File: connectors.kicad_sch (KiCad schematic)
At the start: 9 parts, among them J7001 PinHeader_1x3_P2.54mm_SMD, J7002 PinHeader_1x3_P2.54mm_SMD, J7003 Tag-Connect_TC2050-IDC-NL_2x5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

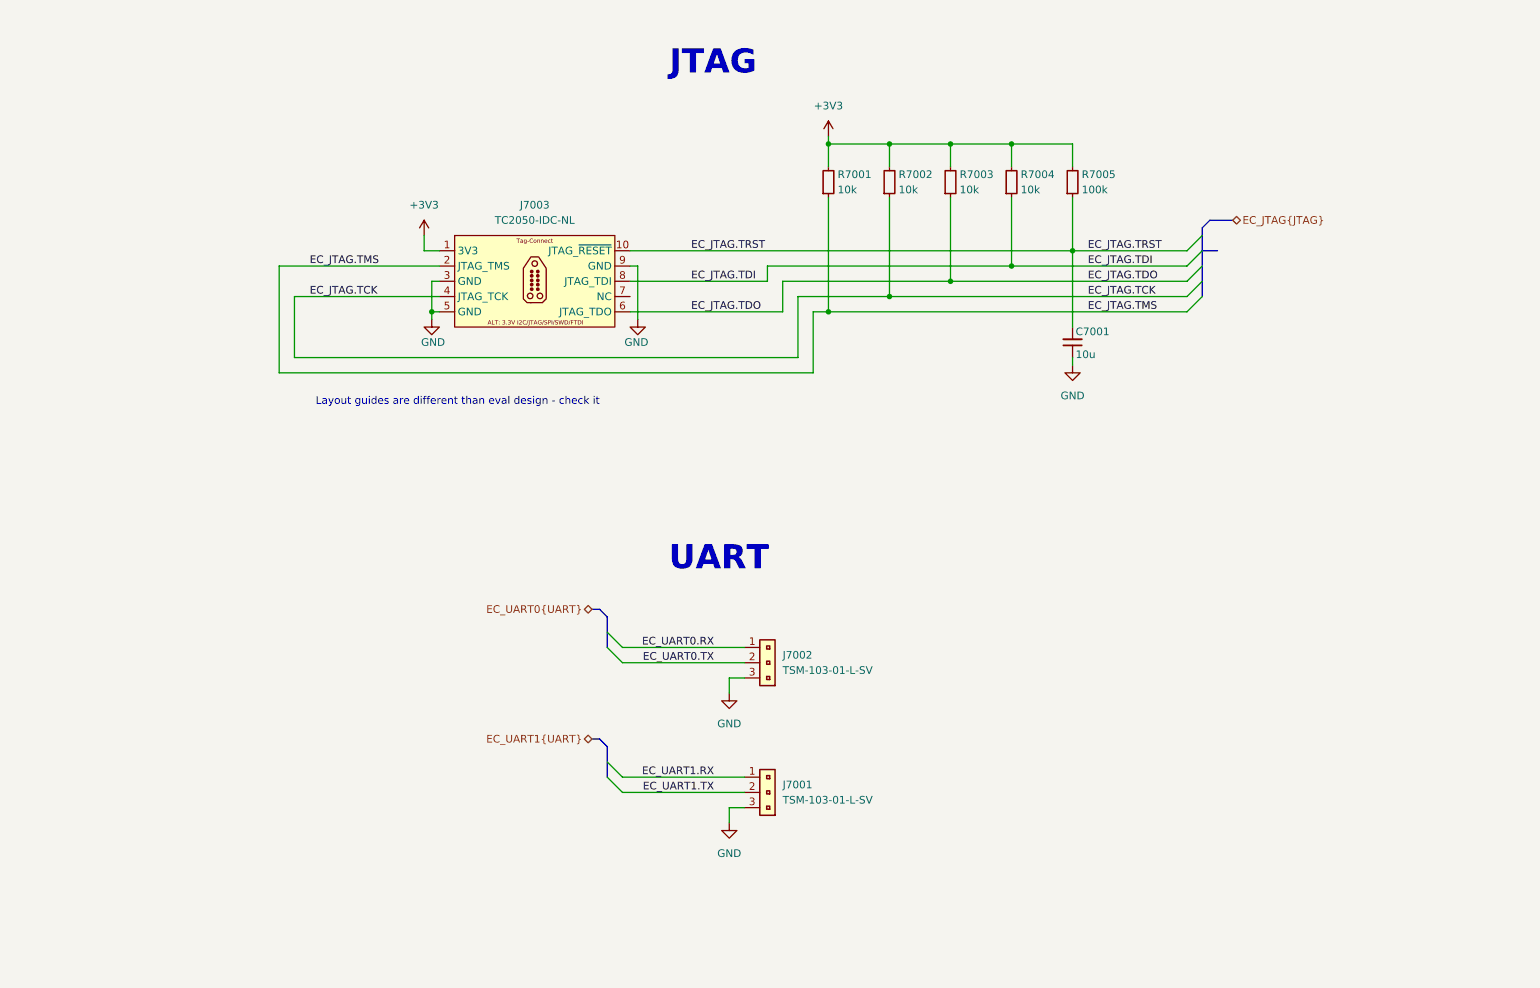
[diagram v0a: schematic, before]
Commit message: [103224] Add USB with FT232RL, transfer elements onto PCB, start positioning elements
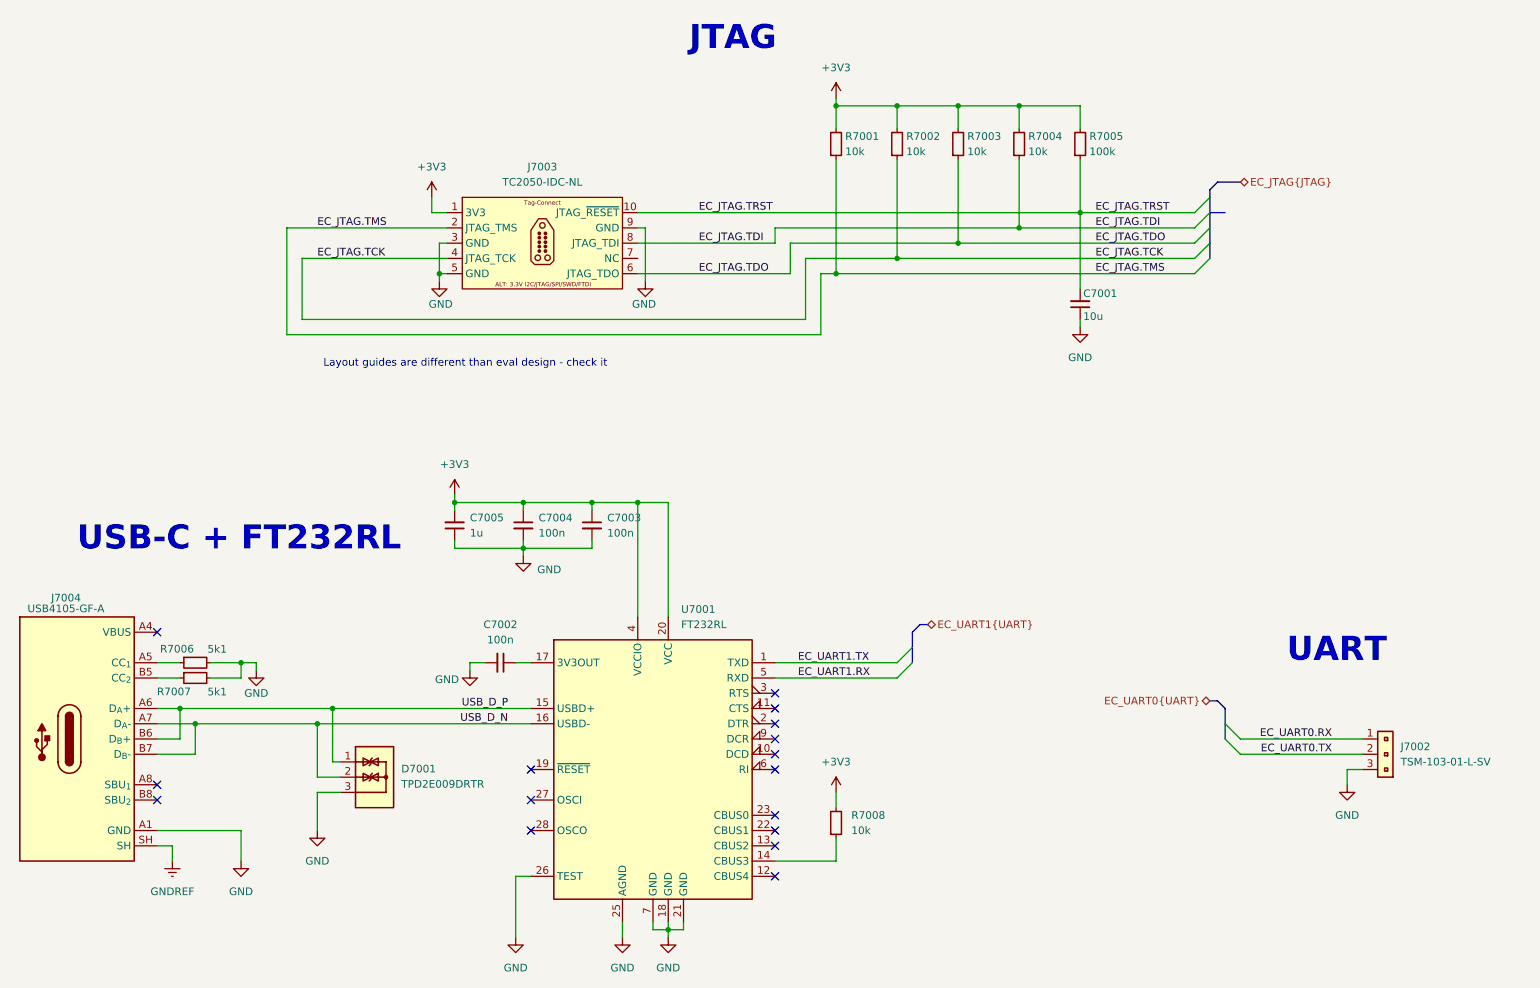
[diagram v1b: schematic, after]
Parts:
- removed J7001: PinHeader_1x3_P2.54mm_SMD, antmicro-footprints:PinHeader_1x3_P2.54mm_SMD, symbol Antmicro Symbols:PinHeader_1x3_P2.54mm_SMD
- added C7002, C7003, C7004: C_100n_0402, antmicro-footprints:C_0402_1005Metric, symbol Capacitors0402:C_100n_0402
- added C7005: C_1u_0603, antmicro-footprints:C_0603_1608Metric, symbol Antmicro Symbols:C_1u_0603
- added D7001: TPD2E009_SOT-9X3, antmicro-footprints:SOT-723, symbol antmicroTVSDiodes:TPD2E009_SOT-9X3
- added J7004: USB-C_GCT_USB4105-GF-A, antmicro-footprints:USB-C_Receptacle_GCT_USB4105-GF-A, symbol antmicroUSBConnectors:USB-C_GCT_USB4105-GF-A
- added R7006, R7007: R_5k1_0402, antmicro-footprints:R_0402_1005Metric, symbol antmicroResistors0402:R_5k1_0402
- added R7008: R_10k_0402, antmicro-footprints:R_0402_1005Metric, symbol Antmicro Symbols:R_10k_0402
- added U7001: FT232RL, Package_SO:SSOP-28_5.3x10.2mm_P0.65mm, symbol Interface_USB:FT232RL
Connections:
- net +3V3: now also C7003.1, C7004.1, C7005.2, R7008.2, U7001.20 (VCC), U7001.4 (VCCIO)
- net EC_UART1.RX: now also U7001.5 (RXD)
- net EC_UART1.TX: now also U7001.1 (TXD)
- net GND: now also C7002.2, C7003.2, C7004.2, C7005.1, D7001.3, J7004.A1 (GND), J7004.A12 (GND), J7004.B1 (GND), J7004.B12 (GND), R7006.2, R7007.2, U7001.18 (GND), U7001.21 (GND), U7001.25 (AGND), U7001.26 (TEST), U7001.7 (GND)
- new net: J7004.B5 (CC_{2}), R7007.1
- new net: J7004.A5 (CC_{1}), R7006.1
- new net: R7008.1, U7001.14 (CBUS3)
- new net: J7004.A4 (VBUS), J7004.A9 (VBUS), J7004.B4 (VBUS), J7004.B9 (VBUS)
- new net: C7002.1, U7001.17 (3V3OUT)
- new net GNDREF: J7004.SH
- new net USB_D_N: D7001.2, J7004.A7 (D_{A}-), J7004.B7 (D_{B}-), U7001.16 (USBD-)
- new net USB_D_P: D7001.1, J7004.A6 (D_{A}+), J7004.B6 (D_{B}+), U7001.15 (USBD+)
- no-connect marks 0 -> 16
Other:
- note added: "USB-C + FT232RL"
- moved on the sheet: C7001, J7002, J7003, R7001, R7002, R7003, R7004, R7005

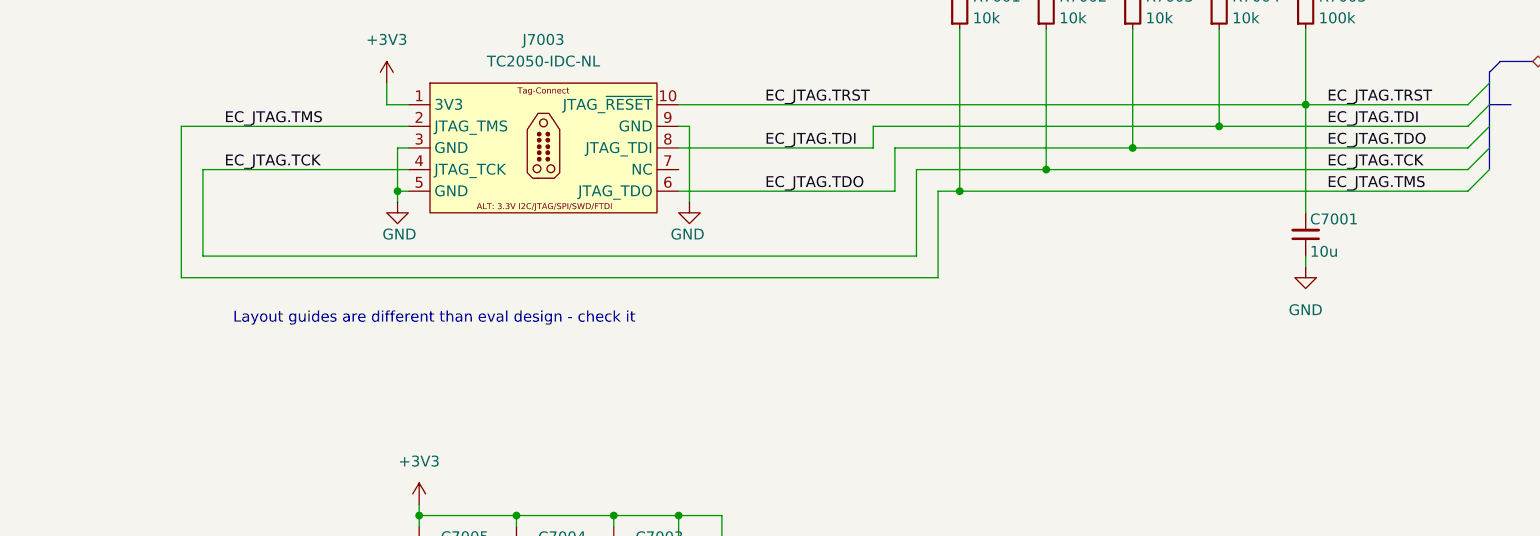
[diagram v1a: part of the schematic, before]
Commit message: [#103696] Add 0 ohm resistors to power rails  on the scheatic, changed C7001 from 10uF to 1uF
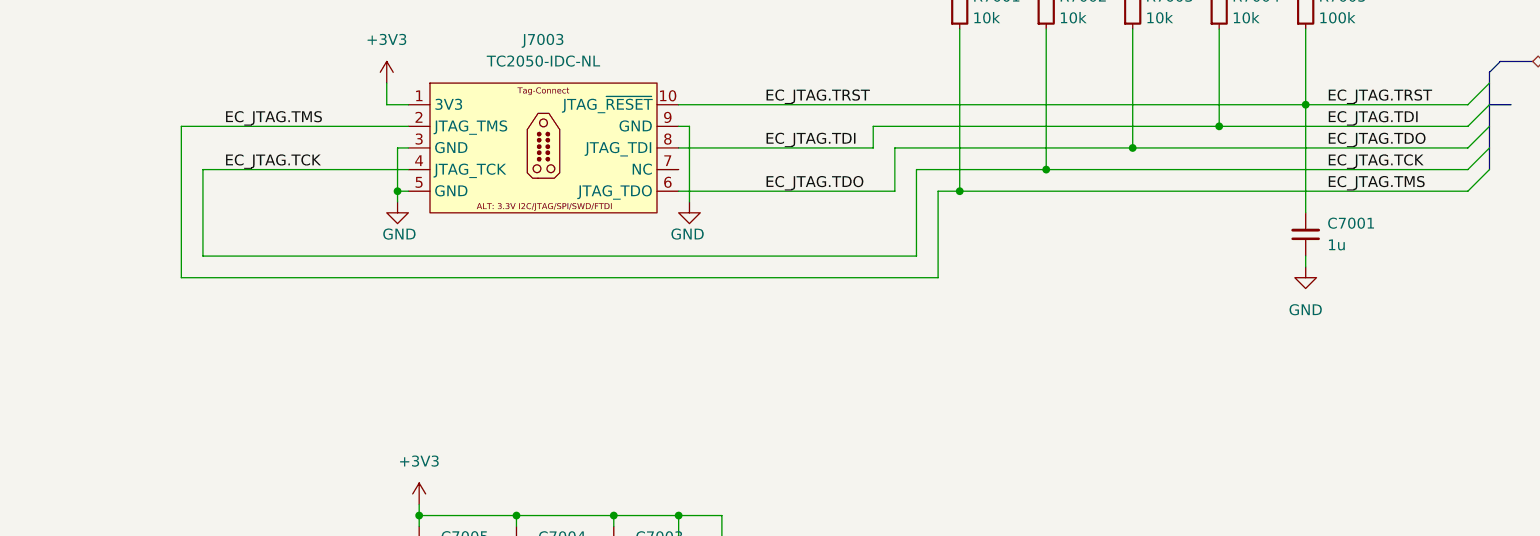
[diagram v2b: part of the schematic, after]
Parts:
- removed C7001: C_10u_10V_X7R_0603, antmicro-footprints:C_0603_1608Metric, symbol Antmicro Symbols:C_10u_10V_X7R_0603
- added C7001: C_1u_0402, antmicro-footprints:C_0402_1005Metric, symbol Antmicro Symbols:C_1u_0402
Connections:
- net EC_JTAG.TRST: now also C7001.2
- net GND: now also C7001.1
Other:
- note removed: "Layout guides are different than eval design - check it"
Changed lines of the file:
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@@
-		)
-	)
-	(text "Layout guides are different than eval design - check it"
-		(exclude_from_sim no)
-		(at 102.108 74.676 0)
-		(effects
-			(font
-				(size 1.27 1.27)
-			)
 		)
 	)
@@
 	)
 	(symbol
-		(lib_id "Antmicro Symbols:C_10u_10V_X7R_0603")
-		(at 204.47 67.31 90)
-		(unit 1)
-		(body_style 1)
-		(exclude_from_sim no)
-		(in_bom yes)
-		(on_board yes)
-		(in_pos_files yes)
-		(dnp no)
-		(property "Reference" "C7001"
-			(at 204.978 62.992 90)
-			(show_name no)
-			(do_not_autoplace no)
-			(effects
-				(font
-					(size 1.27 1.27)
-					(thickness 0.15)
-				)
-				(justify right)
-			)
-		)
-		(property "Value" "C_10u_10V_X7R_0603"
-			(at 214.63 52.07 0)
-			(hide yes)
-			(show_name no)
-			(do_not_autoplace no)
-			(effects
-				(font
-					(size 1.27 1.27)
-					(thickness 0.15)
-				)
-				(justify left bottom)
-			)
-		)
-		(property "Footprint" "antmicro-footprints:C_0603_1608Metric"
-			(at 217.17 52.07 0)
-			(hide yes)
-			(show_name no)
-			(do_not_autoplace no)
-			(effects
-				(font
-					(size 1.27 1.27)
-					(thickness 0.15)
-				)
-				(justify left bottom)
-			)
-		)
-		(property "Datasheet" "https://www.murata.com/products/productdetail?partno=GRM188Z71A106KA73%23"
-			(at 219.71 52.07 0)
-			(hide yes)
-			(show_name no)
-			(do_not_autoplace no)
-			(effects
-				(font
-					(size 1.27 1.27)
-					(thickness 0.15)
-				)
-				(justify left bottom)
-			)
-		)
-		(property "Description" "SMD Multilayer Ceramic Capacitor,  10µF, 10V, 0603, ±10%, X7R"
-			(at 237.49 52.07 0)
-			(hide yes)
-			(show_name no)
-			(do_not_autoplace no)
-			(effects
-				(font
-					(size 1.27 1.27)
-				)
-				(justify left bottom)
-			)
-		)
-		(property "MPN" "GRM188Z71A106KA73D"
-			(at 222.25 52.07 0)
-			(hide yes)
-			(show_name no)
-			(do_not_autoplace no)
-			(effects
-				(font
-					(size 1.27 1.27)
-					(thickness 0.15)
-				)
-				(justify left bottom)
-			)
-		)
-		(property "Val" "10u"
-			(at 204.978 66.802 90)
-			(show_name no)
-			(do_not_autoplace no)
-			(effects
-				(font
-					(size 1.27 1.27)
-					(thickness 0.15)
-				)
-				(justify right)
-			)
-		)
-		(property "Voltage" "10V"
-			(at 224.79 52.07 0)
-			(hide yes)
-			(show_name no)
-			(do_not_autoplace no)
-			(effects
-				(font
-					(size 1.27 1.27)
-					(thickness 0.15)
-				)
-				(justify left bottom)
-			)
-		)
-		(property "Dielectric" "X7R"
-			(at 227.33 52.07 0)
-			(hide yes)
-			(show_name no)
-			(do_not_autoplace no)
-			(effects
-				(font
-					(size 1.27 1.27)
-					(thickness 0.15)
-				)
-				(justify left bottom)
-			)
-		)
-		(property "Manufacturer" "Murata"
-			(at 229.87 52.07 0)
-			(hide yes)
-			(show_name no)
-			(do_not_autoplace no)
-			(effects
-				(font
-					(size 1.27 1.27)
-					(thickness 0.15)
-				)
-				(justify left bottom)
-			)
-		)
-		(property "License" "Apache-2.0"
-			(at 232.41 52.07 0)
-			(hide yes)
-			(show_name no)
-			(do_not_autoplace no)
-			(effects
-				(font
-					(size 1.27 1.27)
-					(thickness 0.15)
-				)
-				(justify left bottom)
-			)
-		)
-		(property "Author" "Antmicro"
-			(at 234.95 52.07 0)
-			(hide yes)
-			(show_name no)
-			(do_not_autoplace no)
-			(effects
-				(font
-					(size 1.27 1.27)
-					(thickness 0.15)
-				)
-				(justify left bottom)
-			)
-		)
-		(pin "1"
-		)
-		(pin "2"
-		)
-		(instances
-			(project "dc-scm-server-integration-espi-adapter"
-				(path "/df391740-647e-4ab6-9dcd-d61184d66fe9/1d8da698-0d26-4a54-ae2a-b123e41282d5"
-					(reference "C7001")
-					(unit 1)
-				)
-			)
-		)
-	)
-	(symbol
 		(lib_id "Antmicro Symbols:R_10k_0402")
 		(at 184.15 40.64 90)
@@
 					(unit 1)
 				)
+			)
+		)
+	)
+	(symbol
+		(lib_id "Antmicro Symbols:C_1u_0402")
+		(at 204.47 67.31 90)
+		(unit 1)
+		(body_style 1)
+		(exclude_from_sim no)
+		(in_bom yes)
+		(on_board yes)
+		(in_pos_files yes)
+		(dnp no)
+		(fields_autoplaced yes)
+		(property "Reference" "C7001"
+			(at 207.01 63.4936 90)
+			(show_name no)
+			(do_not_autoplace no)
+			(effects
+				(font
+					(size 1.27 1.27)
+					(thickness 0.15)
+				)
+				(justify right)
+			)
+		)
+		(property "Value" "C_1u_0402"
+			(at 214.63 46.99 0)
+			(hide yes)
+			(show_name no)
+			(do_not_autoplace no)
+			(effects
+				(font
+					(size 1.27 1.27)
+					(thickness 0.15)
+				)
+				(justify left bottom)
+			)
+		)
+		(property "Footprint" "antmicro-footprints:C_0402_1005Metric"
+			(at 217.17 46.99 0)
+			(hide yes)
+			(show_name no)
+			(do_not_autoplace no)
+			(effects
+				(font
+					(size 1.27 1.27)
+					(thickness 0.15)
+				)
+				(justify left bottom)
+			)
+		)
+		(property "Datasheet" "https://product.tdk.com/en/search/capacitor/ceramic/mlcc/info?part_no=C1005X6S1A105K050BC"
+			(at 219.71 46.99 0)
+			(hide yes)
+			(show_name no)
+			(do_not_autoplace no)
+			(effects
+				(font
+					(size 1.27 1.27)
+					(thickness 0.15)
+				)
+				(justify left bottom)
+			)
+		)
+		(property "Description" "SMD Multilayer Ceramic Capacitor, 1 µF, 10 V, 0402 [1005 Metric], ± 10%, X6S, C"
+			(at 237.49 46.99 0)
+			(hide yes)
+			(show_name no)
+			(do_not_autoplace no)
+			(effects
+				(font
+					(size 1.27 1.27)
+				)
+				(justify left bottom)
+			)
+		)
+		(property "MPN" "C1005X6S1A105K050BC"
+			(at 222.25 46.99 0)
+			(hide yes)
+			(show_name no)
+			(do_not_autoplace no)
+			(effects
+				(font
+					(size 1.27 1.27)
+					(thickness 0.15)
+				)
+				(justify left bottom)
+			)
+		)
+		(property "Manufacturer" "TDK"
+			(at 224.79 46.99 0)
+			(hide yes)
+			(show_name no)
+			(do_not_autoplace no)
+			(effects
+				(font
+					(size 1.27 1.27)
+					(thickness 0.15)
+				)
+				(justify left bottom)
+			)
+		)
+		(property "License" "Apache-2.0"
+			(at 227.33 46.99 0)
+			(hide yes)
+			(show_name no)
+			(do_not_autoplace no)
+			(effects
+				(font
+					(size 1.27 1.27)
+					(thickness 0.15)
+				)
+				(justify left bottom)
+			)
+		)
+		(property "Author" "Antmicro"
+			(at 229.87 46.99 0)
+			(hide yes)
+			(show_name no)
+			(do_not_autoplace no)
+			(effects
+				(font
+					(size 1.27 1.27)
+					(thickness 0.15)
+				)
+				(justify left bottom)
+			)
+		)
+		(property "Val" "1u"
+			(at 207.01 66.0336 90)
+			(show_name no)
+			(do_not_autoplace no)
+			(effects
+				(font
+					(size 1.27 1.27)
+					(thickness 0.15)
+				)
+				(justify right)
+			)
+		)
+		(property "Voltage" ""
+			(at 232.41 46.99 0)
+			(hide yes)
+			(show_name no)
+			(do_not_autoplace no)
+			(effects
+				(font
+					(size 1.27 1.27)
+				)
+				(justify left bottom)
+			)
+		)
+		(property "Dielectric" ""
+			(at 234.95 46.99 0)
+			(hide yes)
+			(show_name no)
+			(do_not_autoplace no)
+			(effects
+				(font
+					(size 1.27 1.27)
+				)
+				(justify left bottom)
+			)
+		)
+		(pin "2"
+		)
+		(pin "1"
+		)
+		(instances
+			(project "dc-scm-server-integration-espi-adapter"
+				(path "/df391740-647e-4ab6-9dcd-d61184d66fe9/1d8da698-0d26-4a54-ae2a-b123e41282d5"
+					(reference "C7001")
+					(unit 1)
+				)

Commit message: [#103811] Replace FT232RL with FT2232H - unifinished
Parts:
- removed C7002: C_100n_0402, antmicro-footprints:C_0402_1005Metric, symbol Capacitors0402:C_100n_0402
- removed C7005: C_1u_0603, antmicro-footprints:C_0603_1608Metric, symbol Antmicro Symbols:C_1u_0603
- added C7002: C_1u_0603, antmicro-footprints:C_0603_1608Metric, symbol Antmicro Symbols:C_1u_0603
- added C7005: C_100n_0402, antmicro-footprints:C_0402_1005Metric, symbol Capacitors0402:C_100n_0402
- added C7006, C7007: C_4u7_10V_X7T_0402, antmicro-footprints:C_0402_1005Metric, symbol Capacitors0402:C_4u7_10V_X7T_0402
- added C7008, C7009, C7010, C7011, C7012, C7013: C_100n_16V_X7R_0402, antmicro-footprints:C_0402_1005Metric, symbol Antmicro Symbols:C_100n_16V_X7R_0402
- added R7009: R_12k_0402, antmicro-footprints:R_0402_1005Metric, symbol Antmicro Symbols:R_12k_0402
- added R7010, R7011: R_10R_0402, antmicro-footprints:R_0402_1005Metric, symbol Antmicro Symbols:R_10R_0402
- added U7002: FT2232HL-REEL, antmicro-footprints:LQFP-64_10x10mm_P0.5mm, symbol Antmicro Symbols:FT2232HL-REEL
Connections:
- net +3V3: now also C7002.2, C7005.1, C7006.2, C7007.2, C7008.2, C7009.2, C7010.2, C7011.2, C7012.2, C7013.2, U7002.20 (VCCIO), U7002.31 (VCCIO), U7002.4 (VPHY), U7002.42 (VCCIO), U7002.56 (VCCIO), U7002.9 (VPLL); no longer C7003.1
- net EC_UART1.RX: no longer U7001.5 (RXD)
- net EC_UART1.TX: no longer U7001.1 (TXD)
- net GND: now also C7002.1, C7005.2, C7006.1, C7007.1, C7008.1, C7009.1, C7010.1, C7011.1, C7012.1, C7013.1, R7009.1, U7002.1 (GND), U7002.10 (AGND), U7002.11 (GND), U7002.15 (GND), U7002.25 (GND), U7002.35 (GND), U7002.47 (GND), U7002.5 (GND), U7002.51 (GND)
- net USB_D_N: no longer D7001.2, J7004.A7 (D_{A}-), J7004.B7 (D_{B}-)
- net USB_D_P: no longer D7001.1, J7004.A6 (D_{A}+), J7004.B6 (D_{B}+)
- net at U7001.17 (3V3OUT): now also C7003.1
- new net: R7009.2, U7002.6 (REF)
- new net: D7001.1, J7004.A6 (D_{A}+), J7004.B6 (D_{B}+), R7010.1
- new net: D7001.2, J7004.A7 (D_{A}-), J7004.B7 (D_{B}-), R7011.1
- new net: U7002.12 (VCORE), U7002.37 (VCORE), U7002.64 (VCORE)
- new net: R7011.2, U7002.7 (DM)
- new net: R7010.2, U7002.8 (DP)
- no-connect marks 16 -> 19
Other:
- note added: "USB-C + FT2232H"
- note removed: "USB-C + FT232RL"
